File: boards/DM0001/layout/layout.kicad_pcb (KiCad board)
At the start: 6 copper layers, 24.9 x 51.5 mm, 147 parts, among them J1 ?, U1 STPS1L40M, U10 LDFPVR, U11 STL180N6F7, U12 STL180N6F7, U13 L6387ED, U14 STL180N6F7, U15 STL180N6F7, U16 L6387ED, U17 STL180N6F7, U18 STL180N6F7, U19 L6387ED, U2 L7986TR, U20 SMM4F26A-TR, U21 SM05B-SRSS-TB, U22 STM32G431C8T6, U23 CSTNE8M00GH5C000R0, U3 LPS4018-333MRC, U4 FSA5157L6X, U5 0435.250KRS, U6 BM05B-SRSS-TB, U7 TCAN330DCNT, U8 BM05B-SRSS-TB, U9 LDFPVR

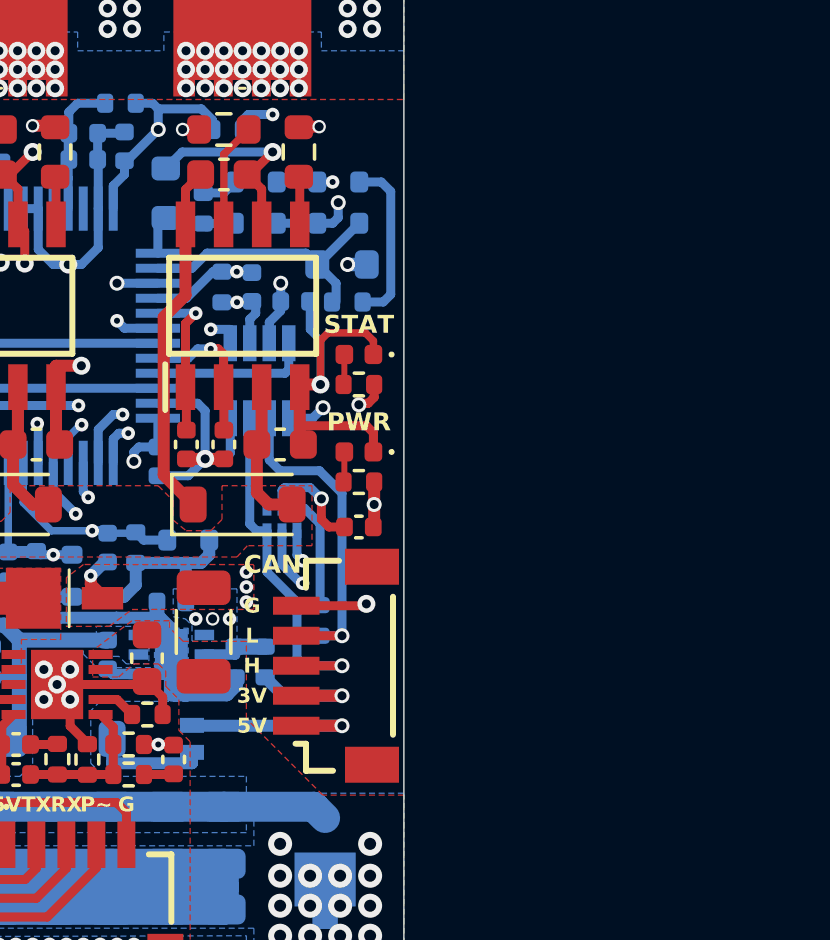
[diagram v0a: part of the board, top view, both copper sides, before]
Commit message: remove ignored files
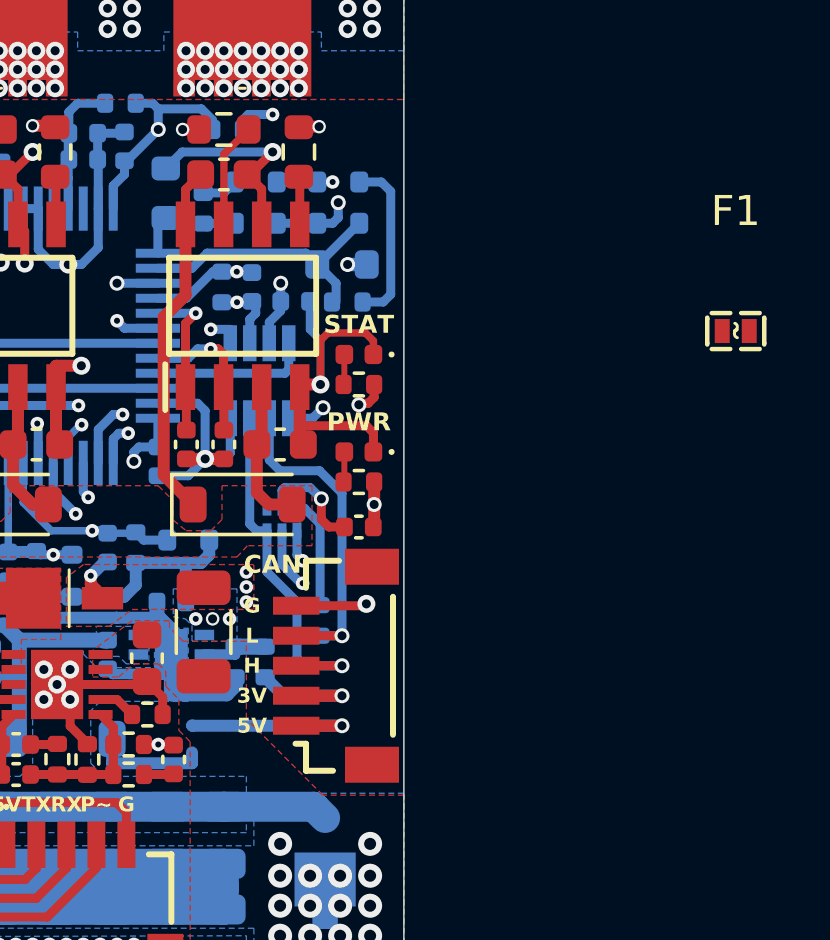
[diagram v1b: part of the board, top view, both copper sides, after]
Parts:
- removed U5: 0435.250KRS, F0402:F0402
- added F1: 0435.250KRS, F0402:F0402, F.Cu at (90.7, 106.4)
- renumbered U1 to D1, D9 to D10, D10 to D11, D11 to D12, D12 to D13, D13 to D14, D14 to D15, D15 to D16, D16 to D17, D1 to D2, D2 to D3, D3 to D4, D4 to D5, D5 to D6, D6 to D7, D7 to D8, D8 to D9, U7 to IC1, U9 to IC2, U10 to IC3, U13 to IC4, U16 to IC5, U19 to IC6, U22 to IC7, U6 to J1, U8 to J2, U21 to J3, J1 to J4, U3 to L1, U2 to PS1, U11 to Q1, U12 to Q2, U14 to Q3, U15 to Q4, U17 to Q5, U18 to Q6, U4 to S1, U23 to Y1, U20 to Z1

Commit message: update stdlib
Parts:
- F1: moved to B.Cu
- moved F1 16.3 mm to (82.4, 120.4), turned to 90 degrees
- moved C1 9.90 mm to (82.8, 116.9)
- moved C10 9.90 mm to (85.9, 105.8)
- moved C11 9.90 mm to (79.6, 114.0)
- moved C12 9.90 mm to (76.3, 114.7)
- moved C13 9.90 mm to (75.4, 114.7)
- moved C14 9.90 mm to (68.3, 119.5)
- moved C15 9.90 mm to (79.6, 117.6)
- moved C16 9.90 mm to (81.7, 115.9)
- moved C2 9.90 mm to (80.9, 117.7)
- moved C24 9.90 mm to (76.0, 88.1)
- moved C25 9.90 mm to (75.4, 101.6)
- moved C26 9.90 mm to (75.4, 110.6)
- moved C27 9.90 mm to (74.1, 110.6)
- moved C28 9.90 mm to (77.2, 110.6)
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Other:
- board text added: "0.0152 mm"
- board text added: "0.025"
- board text added: "0.0900 mm / 0.0900 mm"
- board text added: "0.0994 mm"
- board text added: "0.1164 mm"
- board text added: "0.1500 mm"
- board text added: "0.55 mm"
- board text added: "2116"
- board text added: "3313"
- board text added: "4.1"
- board text added: "4.16"
- board text added: "4.6"
- board text added: "Black"
- board text added: "ENIG"
- board text added: "FR4-Core"
- board text added: "White"
- board text removed: "0.02"
- board text removed: "0.1 mm"
- board text removed: "0.1600 mm / 0.2000 mm"
- board text removed: "0.2000 mm"
- board text removed: "0.535 mm"
- board text removed: "4.5"
- board text removed: "FR4"
- board text removed: "None"

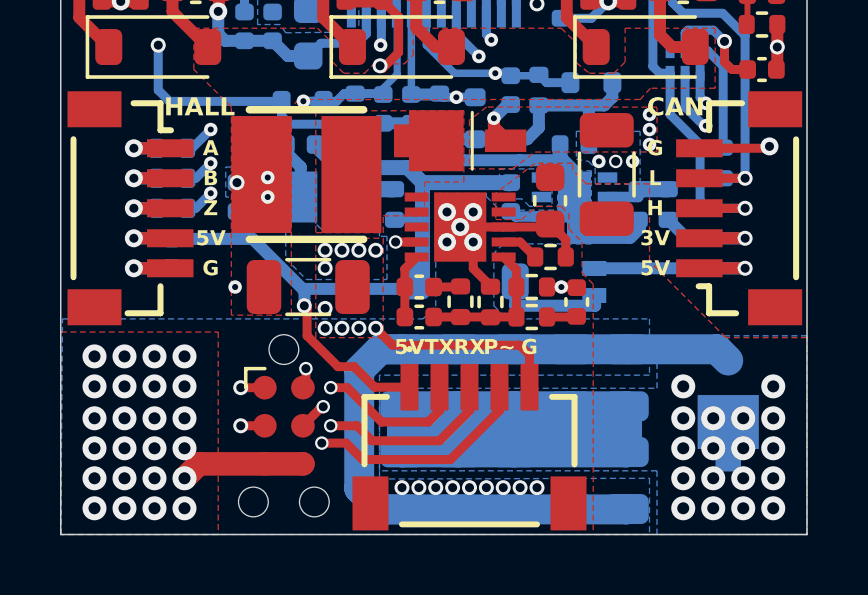
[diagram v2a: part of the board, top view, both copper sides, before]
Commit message: pad markings
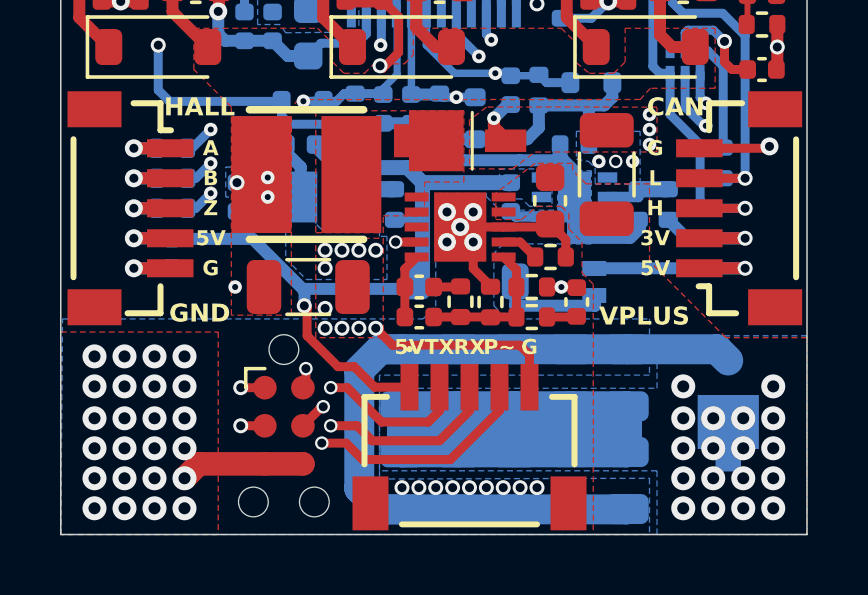
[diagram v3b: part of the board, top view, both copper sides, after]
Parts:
- C10, C14, C44, C45, C47, C50, C8, C9: value 100nF 16V X7R -> GCM155R71H104KE02D
- C11, C12, C13: value 10pF 10V -> GCM1555C1H100FA16D
- C2: value 220nF 50V X7R -> GCM188R71H224KA64D
- C20, C25, C30: value 1uF 25V -> GCM188R71E105KA64D
- C21, C22, C26, C27, C31, C32: value 100pF 10V -> GCM1555C1H101FA16D
- C4: value 27pF 25V -> GCM1555C1H300FA16D
- C46: value 4.7uF 10V X5R -> GRM188Z71C475KE21D
- C49: value 10nF 16V X7R -> GRM1555CYA103GE01D
- D16: value LED GREEN -> VLMG1500-GS08
- D17: value LED RED -> VLMS1500-GS08
- R1: value 4.7k -> ERJ-2RKF4701X
- R10, R11, R12, R13, R15, R19, R21, R27, R29, R35, R37, R7, R8, R9: value 10k -> ERJ-2RKF1002X
- R14: value 30.9k -> ERJ-2RKF3092X
- R16: value 52.3k -> ERJ-2RKF5232X
- R17, R25, R33: value 2.2k -> ERJ-2RKF2201X
- R18, R20, R26, R28, R34, R36: value 33 -> ERJ-3EKF33R0V
- R2: value 300 -> ERJ-2RKF3000X
- R22, R30, R38: value 10k -> ERJ-3EKF1002V
- R24, R32, R40: value 3m 1% -> CSNL2512FT3L00
- R3: value 34.8k -> ERJ-2RKF3482X
- R4: value 8.2k -> ERJ-2RKF8201X
- R41, R42: value 1k 1% -> ERJ-2RKF1001X
- R43: value 4.7k 1% -> ERJ-2RKF4701X
- R44: value 18k 1% -> ERJ-2RKF1802X
- R45: value 169k 1% -> ERJ-2RKF1693X
- R46: value 220 -> ERJ-2RKF2200X
- R47, R48, R49: value 2.2k 1% -> ERJ-2RKF2201X
- R5: value 62 -> ERJ-2RKF62R0X
- R50, R51, R52: value 22k 1% -> ERJ-2RKF2202X
- R53, R54, R55: value 1.5k 1% -> ERJ-2RKF1501X
- R6: value 120 1% -> ERJ-2RKF1200X
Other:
- board text added: "GND"
- board text added: "VPLUS"
